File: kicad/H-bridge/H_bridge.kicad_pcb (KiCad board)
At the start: 2 copper layers, 127 x 63.5 mm, 69 parts, among them J1 Screw_Terminal_01x03, J2 Conn_Coaxial, J3 2453710000, J4 Screw_Terminal_01x02, Q1 IAUT300N10S5N014ATMA1, Q2 IAUT300N10S5N014ATMA1, Q3 IAUT300N10S5N014ATMA1, Q4 IAUT300N10S5N014ATMA1, U1 LTV-817, U2 PDS1-S15-S15-M, U3 HIP4080A, U4 LT1011, U5 LM340MPX-5.0/NOPB, U6 74LVC1G373, U8 74AC14DR

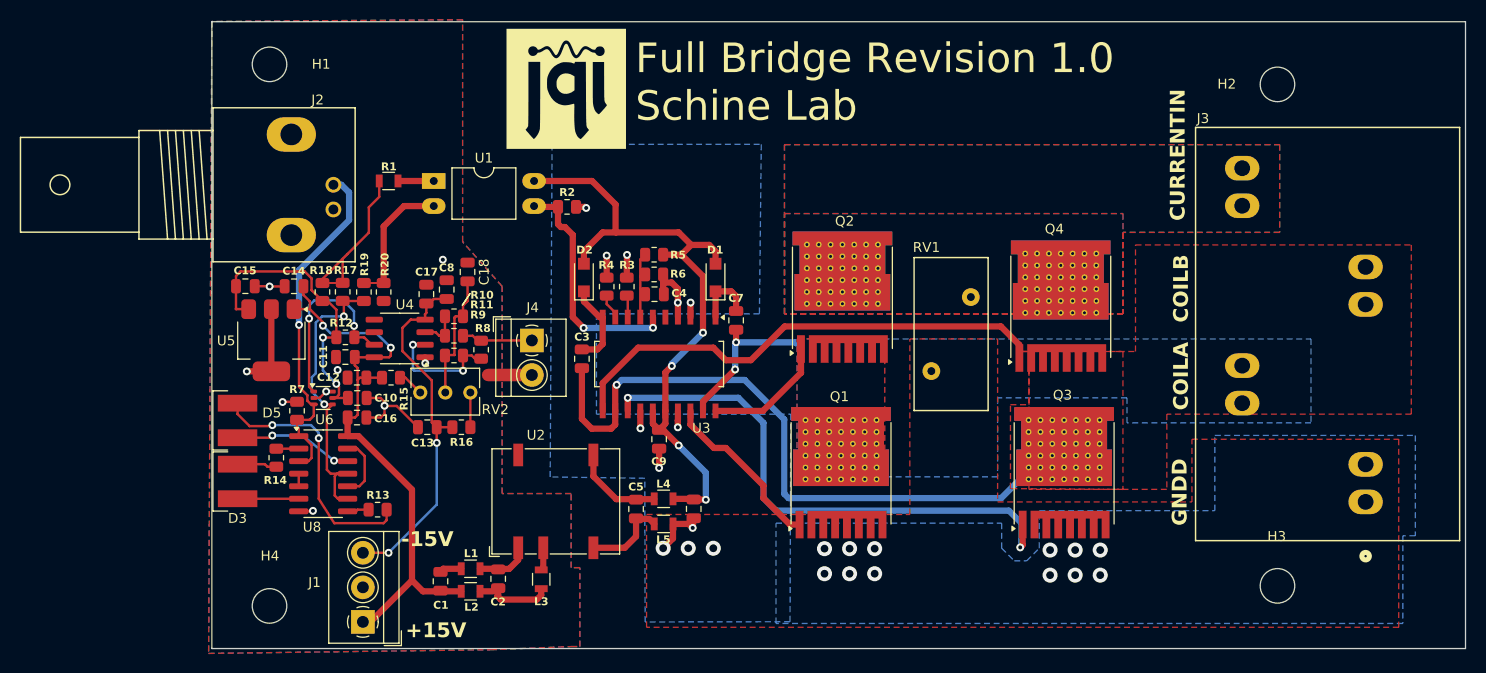
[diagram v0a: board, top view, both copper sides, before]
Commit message: Trimportand INverter power supply fix, now connects to 5V
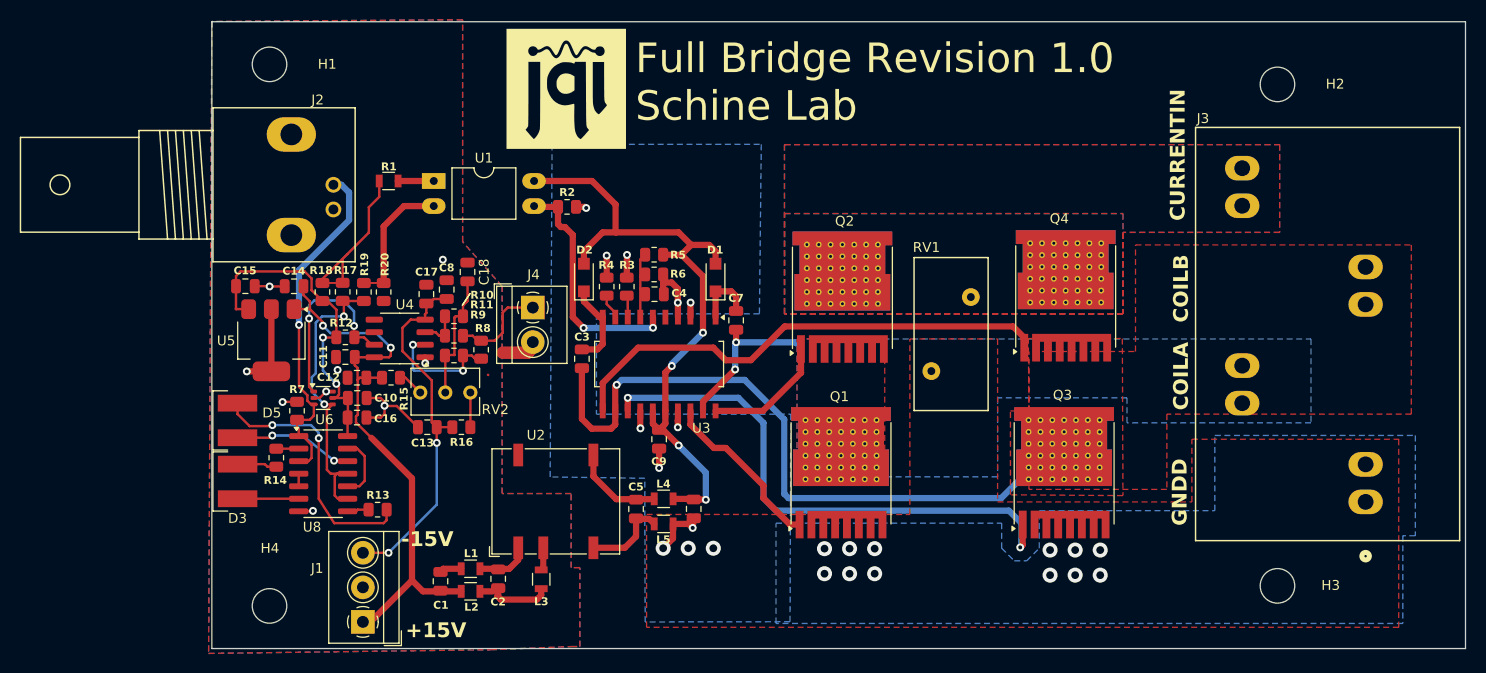
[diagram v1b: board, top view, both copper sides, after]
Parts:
- moved J4 3.34 mm to (134.1, 105.2)
- moved Q4 1.16 mm to (188.1, 104.0)
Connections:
- C16 pad 2: VCC -> +5V
- U8 pad 14: VCC -> +5V
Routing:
- net +5V: track 30.3 -> 34.2 mm
- net /protection/monitor: track 7.20 -> 9.89 mm
- net VCC: track 60.7 -> 58.9 mm
- net GND: track 34.0 -> 33.4 mm
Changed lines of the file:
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@@
 	(footprint "Package_TO_SOT_SMD:Infineon_PG-HSOF-8-1_ThermalVias"
 		(layer "F.Cu")
-		(at 187.59842 105.016656 90)
+		(at 188.096 103.97 90)
 		(descr "HSOF-8-1 [TOLL] power MOSFET (http://www.infineon.com/cms/en/product/packages/PG-HSOF/PG-HSOF-8-1/)")
 		(tags "mosfet hsof toll thermal vias")
@@
 			(layers "F.Cu" "F.Paste" "F.Mask")
 			(roundrect_rratio 0.25)
-			(net 22 "VCC")
+			(net 42 "+5V")
 			(pinfunction "VCC")
 			(pintype "power_in")
@@
 			(layers "F.Cu" "F.Paste" "F.Mask")
 			(roundrect_rratio 0.25)
-			(net 22 "VCC")
+			(net 42 "+5V")
 			(pintype "passive")
 		)
@@
 		(tags "mounting hole 3.5mm no annular")
 		(property "Reference" "H3"
-			(at -0.078 -5.012 0)
+			(at 5.391121 -0.053066 0)
 			(layer "F.SilkS")
 			(effects
@@
 		(tags "mounting hole 3.5mm no annular")
 		(property "Reference" "H1"
-			(at 5.228 -0.018 0)
+			(at 5.842 -0.018 0)
 			(layer "F.SilkS")
 			(effects
@@
 		(tags "THT Terminal Block 4Ucon ItemNo. 20193 pitch 3.5mm size 11.2x7mm^2 drill 1.2mm pad 2.4mm")
 		(property "Reference" "J1"
-			(at 4 -4.9 180)
+			(at 5.428 -4.632 180)
 			(layer "F.SilkS")
 			(effects
@@
 	(footprint "TerminalBlock_4Ucon:TerminalBlock_4Ucon_1x02_P3.50mm_Horizontal"
 		(layer "F.Cu")
-		(at 134.02 108.49 -90)
+		(at 134.112 105.156 -90)
 		(descr "Terminal Block 4Ucon ItemNo. 19963, 2 pins, pitch 3.5mm, size 7.7x7mm^2, drill diamater 1.2mm, pad diameter 2.4mm, see http://www.4uconnector.com/online/object/4udrawing/19963.pdf, script-generated using https://github.com/pointhi/kicad-footprint-generator/scripts/TerminalBlock_4Ucon")
 		(tags "THT Terminal Block 4Ucon ItemNo. 19963 pitch 3.5mm size 7.7x7mm^2 drill 1.2mm pad 2.4mm")
@@
 		(tags "mounting hole 3.5mm no annular")
 		(property "Reference" "H2"
-			(at -5.138 -0.038 0)
+			(at 5.842 -0.038 0)
 			(layer "F.SilkS")
 			(effects
@@
 		(tags "mounting hole 3.5mm no annular")
 		(property "Reference" "H4"
-			(at 0.038 -5.072 0)
+			(at 0.038 -5.842 0)
 			(layer "F.SilkS")
 			(effects
@@
 	(dimension
 		(type aligned)
-		(layer "F.SilkS")
+		(layer "Dwgs.User")
 		(pts
-			(xy 209.55 135.89) (xy 215.90827 135.866743)
+			(xy 101.6 139.7) (xy 209.55 139.64)
 		)
-		(height 0.0993)
-		(gr_text "0.2503 in"
-			(at 212.725291 134.827678 0.2095820556)
-			(layer "F.SilkS")
+		(height -3.651785)
+		(gr_text "107.9500 mm"
+			(at 155.572331 134.868216 0.03184572873)
+			(layer "Dwgs.User")
 			(effects
 				(font
@@
 		(layer "Dwgs.User")
 		(pts
-			(xy 101.6 139.7) (xy 209.55 139.64)
+			(xy 101.6 139.7) (xy 215.804976 139.668123)
 		)
-		(height -3.651785)
-		(gr_text "4.2500 in"
-			(at 155.572331 134.868216 0.03184572873)
+		(height 0.020062)
+		(gr_text "114.2050 mm"
+			(at 158.702173 138.554123 0.01599295299)
 			(layer "Dwgs.User")
 			(effects
@@
 		(layer "Dwgs.User")
 		(pts
-			(xy 101.6 139.7) (xy 215.804976 139.668123)
+			(xy 209.55 135.89) (xy 215.90827 135.866743)
 		)
-		(height 0.020062)
-		(gr_text "4.4963 in"
-			(at 158.702173 138.554123 0.01599295299)
+		(height 0.0993)
+		(gr_text "6.3583 mm"
+			(at 212.725291 134.827678 0.2095820556)
 			(layer "Dwgs.User")
 			(effects
@@
 		)
 		(height 9.683539)
-		(gr_text "2.4992 in"
+		(gr_text "63.4800 mm"
 			(at 239.441301 107.937334 -89.98598654)
 			(layer "Dwgs.User")
@@
 		)
 		(height 7.210214)
-		(gr_text "5.0006 in"
+		(gr_text "127.0155 mm"
 			(at 165.108719 145.750197 0.009037191542)
 			(layer "Dwgs.User")
@@
 	)
 	(segment
+		(start 133.604 109.728)
+		(end 131.064 109.728)
+		(width 1.27)
+		(layer "F.Cu")
+		(net 1)
+	)
+	(segment
 		(start 110.227172 114.705146)
 		(end 108.78612 114.705146)
@@
 	)
 	(segment
-		(start 134.02 111.99)
-		(end 129.59 111.99)
-		(width 1.27)
-		(layer "F.Cu")
-		(net 1)
-	)
-	(segment
 		(start 119.08961 115.926656)
 		(end 119.08961 115.101656)
@@
 	)
 	(segment
+		(start 134.112 108.656)
+		(end 134.112 109.22)
+		(width 1.27)
+		(layer "F.Cu")
+		(net 1)
+	)
+	(segment
 		(start 107.627172 111.617646)
 		(end 105.14862 111.617646)
@@
 	)
 	(segment
+		(start 134.112 109.22)
+		(end 133.604 109.728)
+		(width 1.27)
+		(layer "F.Cu")
+		(net 1)
+	)
+	(segment
 		(start 118.7056 114.317646)
 		(end 119.06461 114.676656)
@@
 	)
 	(segment
-		(start 115.353642 116.300706)
-		(end 115.353642 118.175797)
-		(width 0.635)
-		(layer "F.Cu")
-		(net 22)
-	)
-	(segment
 		(start 118.836635 112.264077)
 		(end 117.249135 112.264077)
@@
 	)
 	(segment
-		(start 115.353642 118.175797)
-		(end 115.351477 118.177962)
+		(start 116.377172 116.017646)
+		(end 116.197409 116.197409)
 		(width 0.25)
 		(layer "F.Cu")
@@
 	)
 	(segment
-		(start 119.552172 110.192646)
-		(end 119.727172 110.017646)
+		(start 116.197409 116.197409)
+		(end 116.197409 116.789573)
 		(width 0.25)
 		(layer "F.Cu")
@@
 	)
 	(segment
-		(start 116.094112 116.300706)
-		(end 115.353642 116.300706)
+		(start 119.552172 110.192646)
+		(end 119.727172 110.017646)
 		(width 0.25)
 		(layer "F.Cu")
@@
 	)
 	(segment
-		(start 122.98461 133.903656)
-		(end 124.74661 133.903656)
+		(start 121.874396 132.793442)
+		(end 121.874396 122.46656)
 		(width 0.635)
 		(layer "F.Cu")
@@
 	)
 	(segment
-		(start 111.527477 104.527477)
-		(end 110.877172 103.877172)
-		(width 0.25)
-		(layer "F.Cu")
-		(net 22)
-	)
-	(segment
-		(start 116.453635 118.177962)
-		(end 115.351477 118.177962)
+		(start 122.98461 133.903656)
+		(end 124.74661 133.903656)
 		(width 0.635)
 		(layer "F.Cu")
@@
 	)
 	(segment
-		(start 121.874396 123.598723)
-		(end 116.453635 118.177962)
-		(width 0.635)
+		(start 111.527477 104.527477)
+		(end 110.877172 103.877172)
+		(width 0.25)
 		(layer "F.Cu")
 		(net 22)
 	)
 	(segment
-		(start 121.874396 132.793442)
-		(end 121.874396 123.598723)
+		(start 117.667838 137)
+		(end 116.9 137)
 		(width 0.635)
 		(layer "F.Cu")
@@
 	)
 	(segment
-		(start 117.667838 137)
-		(end 116.9 137)
-		(width 0.635)
+		(start 116.197409 116.789573)
+		(end 117.755836 118.348)
+		(width 0.25)
 		(layer "F.Cu")
 		(net 22)
@@
 	)
 	(segment
-		(start 116.377172 116.017646)
-		(end 116.094112 116.300706)
-		(width 0.25)
-		(layer "F.Cu")
-		(net 22)
-	)
-	(segment
 		(start 124.77861 133.903656)
 		(end 124.76261 133.887656)
@@
 		(net 22)
 	)
+	(segment
+		(start 121.874396 122.46656)
+		(end 117.755836 118.348)
+		(width 0.635)
+		(layer "F.Cu")
+		(net 22)
+	)
 	(via
 		(at 119.727172 109.217646)
@@
 	)
 	(segment
-		(start 159.628703 107.071297)
-		(end 181.536458 107.071297)
+		(start 141.19342 112.80658)
+		(end 144.78 109.22)
 		(width 0.635)
 		(layer "F.Cu")
@@
 	)
 	(segment
-		(start 153.67 110.49)
-		(end 156.21 110.49)
+		(start 144.78 109.22)
+		(end 152.4 109.22)
 		(width 0.635)
 		(layer "F.Cu")
@@
 	)
 	(segment
-		(start 141.19342 112.80658)
-		(end 144.78 109.22)
+		(start 156.21 110.49)
+		(end 159.628703 107.071297)
 		(width 0.635)
 		(layer "F.Cu")
@@
 	)
 	(segment
-		(start 183.39842 108.933259)
-		(end 183.39842 110.266656)
+		(start 183.896 108.204)
+		(end 183.896 109.22)
 		(width 0.635)
 		(layer "F.Cu")
@@
 	)
 	(segment
-		(start 144.78 109.22)
-		(end 152.4 109.22)
+		(start 159.628703 107.071297)
+		(end 182.763297 107.071297)
 		(width 0.635)
 		(layer "F.Cu")
@@
 	)
 	(segment
-		(start 181.536458 107.071297)
-		(end 183.39842 108.933259)
+		(start 182.763297 107.071297)
+		(end 183.896 108.204)
 		(width 0.635)
 		(layer "F.Cu")
@@
 	)
 	(segment
-		(start 156.21 110.49)
-		(end 159.628703 107.071297)
+		(start 153.67 110.49)
+		(end 156.21 110.49)
 		(width 0.635)
 		(layer "F.Cu")
@@
 	)
 	(segment
+		(start 115.351477 116.302871)
+		(end 115.353642 116.300706)
+		(width 0.25)
+		(layer "F.Cu")
+		(net 42)
+	)
+	(segment
 		(start 113.827172 114.317646)
 		(end 114.152171 114.317646)
@@
 	)
 	(segment
+		(start 115.377172 114.317646)
+		(end 115.377172 116.277176)
+		(width 0.25)
+		(layer "F.Cu")
+		(net 42)
+	)
+	(segment
 		(start 113.332072 104.492646)
 		(end 114.214672 105.375246)
@@
 	)
 	(segment
+		(start 115.351477 118.177962)
+		(end 115.351477 116.302871)
+		(width 0.25)
+		(layer "F.Cu")
+		(net 42)
+	)
+	(segment
 		(start 104.038487 105.303902)
 		(end 104.052231 105.317646)
@@
 	)
 	(segment
+		(start 115.377172 116.277176)
+		(end 115.353642 116.300706)
+		(width 0.25)
+		(layer "F.Cu")
+		(net 42)
+	)
+	(segment
 		(start 104.045796 102.994517)
 		(end 104.045796 105.296593)
@@
 	)
 	(segment
+		(start 131.064 105.664)
+		(end 131.572 105.156)
+		(width 0.25)
+		(layer "F.Cu")
+		(net 48)
+	)
+	(segment
 		(start 128.527172 108.514077)
 		(end 128.027172 108.014077)
@@
 	)
 	(segment
-		(start 134.02 108.49)
-		(end 128.901249 108.49)
+		(start 131.064 107.696)
+		(end 131.064 105.664)
 		(width 0.25)
 		(layer "F.Cu")
@@
 		(net 48)
 	)
+	(segment
+		(start 128.877172 108.514077)
+		(end 130.245923 108.514077)
+		(width 0.25)
+		(layer "F.Cu")
+		(net 48)
+	)
+	(segment
+		(start 130.245923 108.514077)
+		(end 131.064 107.696)
+		(width 0.25)
+		(layer "F.Cu")
+		(net 48)
+	)
+	(segment
+		(start 131.572 105.156)
+		(end 134.112 105.156)
+		(width 0.25)
+		(layer "F.Cu")
+		(net 48)
+	)
 	(zone
 		(net 0)
@@
 		(polygon
 			(pts
-				(xy 182.5 115) (xy 184.379676 115) (xy 184.37342 109.606656) (xy 193.89842 109.606656) (xy 193.89842 123.576656)
-				(xy 182.5 123.5)
+				(xy 182.5 115.629344) (xy 184.379676 115.629344) (xy 184.308889 108.296477) (xy 193.833889 108.296477)
+				(xy 193.89842 124.206) (xy 182.5 124.129344)
 			)
 		)
@@
 				(xy 212.423852 136.203852) (xy 212.690769 135.909356) (xy 212.927534 135.590114) (xy 213.131868 135.249203)
 				(xy 213.301804 134.889906) (xy 213.435703 134.515682) (xy 213.532277 134.130135) (xy 213.590597 133.736979)
-				(xy 213.610099 133.34)
 			)
 		)
